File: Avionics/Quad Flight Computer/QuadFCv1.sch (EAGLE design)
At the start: 120 parts, among them J1 10104111_MICROUSBAB, J2 1050270001, Q1 DMP2035U, Q2 DMP2035U, Q3 DMP2035U, SW1 2-1437565-9, U1 TM4C123GH6PZ, U10 LTC4412, U11 AP7215-33YG-13, U2 74LVC4245APW, U3 ATMEGA32U2-MU, U4 SPI_PPM, U5 MPU-6000, U6 HMC5883LSMD, U7 MS5611-01BA, U8 74AUP1G19GW, U9 S25FL127S, X1 HWB, Y1 32.768KHZ, Y2 AWSCR-20.00CW-T, Y3 PRQC16.00SR5010X000

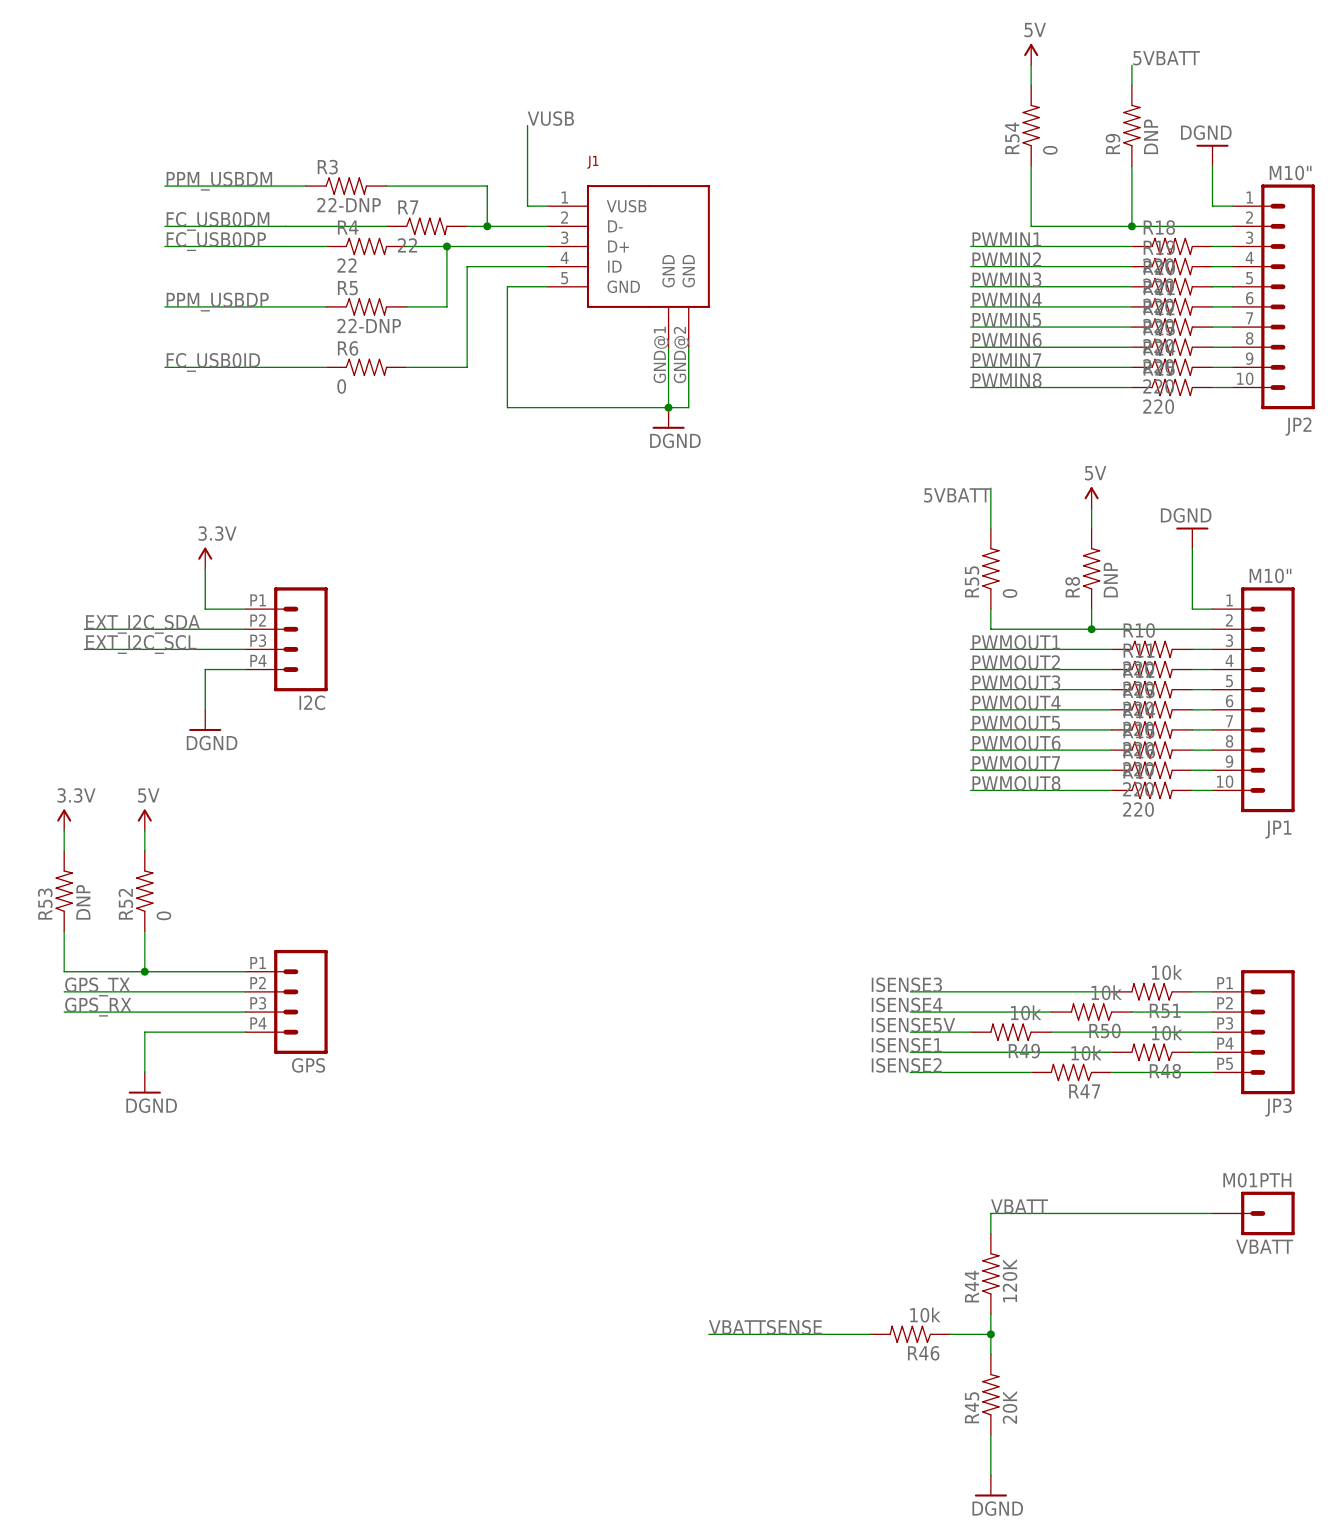
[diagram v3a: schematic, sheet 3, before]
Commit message: Changed form factor of FC to be 1.95"x1.95" to be compliant with the power distribution board. Makes stacking and interconnectivity simpler.
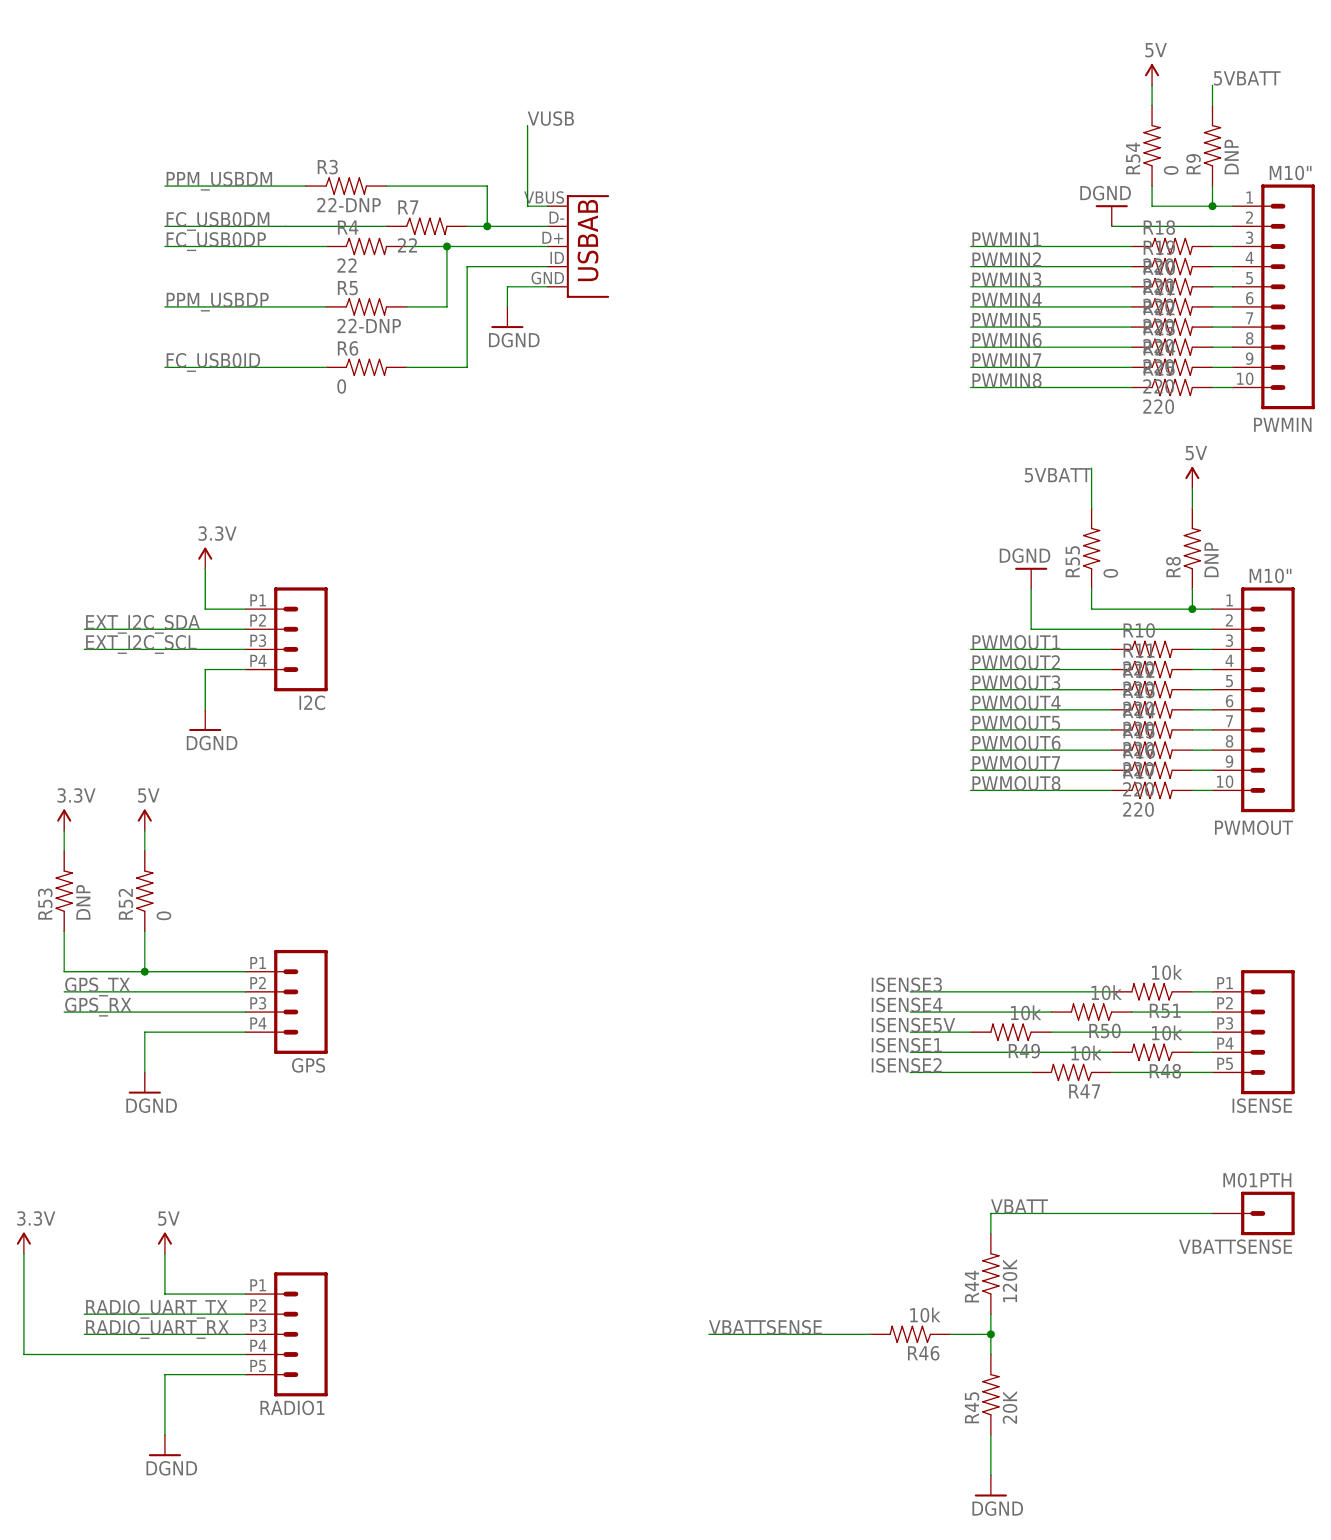
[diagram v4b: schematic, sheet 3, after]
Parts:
- removed J1: 10104111_MICROUSBAB, Shared Libraries:10104111_MICROUSBAB
- removed U4: SPI_PPM, SparkFunv2:AVR_SPI_PRG_6NS
- added RADIO1: (no value), Shared Libraries:M05DF13
- added SPI_PPM: SPI_PPM, Shared Libraries:M03X2SMD_0.05
- added U12: (no value), SparkFun-Connectors:USB-AB
- C24: device SparkFun-Capacitors:CAP0603-CAP -> SparkFun-Capacitors:CAP0402-CAP
- FC_JTAG: value M04X2 -> M04X2SMT-0.05; device SparkFun-Connectors:M04X2 -> Shared Libraries:M04X2SMT-0.05
- renumbered JP1 to PWMOUT, JP2 to PWMIN, JP3 to ISENSE, VBATT to VBATTSENSE
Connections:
- new net RADIO_UART_RX: RADIO1.3
- new net RADIO_UART_TX: RADIO1.2
- net 3.3V: now also RADIO1.4
- net 5V: now also RADIO1.1, SPI_PPM.2; no longer U4.2
- net GND: now also PWMIN.2, PWMOUT.2, RADIO1.5, SPI_PPM.6, U12.GND; no longer J1.GND, J1.GND@1, J1.GND@2, PWMIN.1, PWMOUT.1, U4.6
- net N$23: now also PWMIN.1; no longer PWMIN.2
- net N$26: now also PWMOUT.1; no longer PWMOUT.2
- net N$27: now also U12.USBID; no longer J1.ID
- net N$28: now also U12.D-; no longer J1.D-
- net N$29: now also U12.D+; no longer J1.D+
- net PPM_RST: now also SPI_PPM.5; no longer U4.5
- net PWMIN2: now also SPI_PPM.3; no longer U4.3
- net PWMIN3: now also SPI_PPM.4; no longer U4.4
- net PWMIN4: now also SPI_PPM.1; no longer U4.1
- net VUSB: now also U12.VBUS; no longer J1.VUSB
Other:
- moved on the sheet: R54, R55, R8, R9

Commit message: Consolidated entire design into single FC library. Makes everything neater and avoids package conflicts. Using any new package should be added to this library OR copied to it from another lib.
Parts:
- removed TP2: TPSQTP10SQ, testpad:TPSQTP10SQ
- added BZR: CMT-1203-SMT, QuadFCv1:CMT-1203-SMT
- added PPM: TESTPAD_TPSQTP10SQ, QuadFCv1:TESTPAD_TPSQTP10SQ
- C1, C10, C11, C12, C13, C14, C15, C16, C17, C18, C19, C2, C20, C21, C22, C23, C24, C25, C26, C3, C4, C5, C6, C7, C8, C9: device SparkFun-Capacitors:CAP0402-CAP -> QuadFCv1:CAP0402-CAP
- F1: device SparkFun:PTCSMD -> QuadFCv1:PTC0603
- FC_JTAG: device Shared Libraries:M04X2SMT-0.05 -> QuadFCv1:M04X2SMT-0.05
- GPS, I2C: device Shared Libraries:M04DF13 -> QuadFCv1:M04DF13
- ISENSE, RADIO1: device Shared Libraries:M05DF13 -> QuadFCv1:M05DF13
- J2: device Shared Libraries:1050270001 -> QuadFCv1:1050270001
- L1: device SparkFun-Passives:INDUCTOR0603 -> QuadFCv1:INDUCTOR0603
- LED1, LED2, LED3: device SparkFun:LED0603 -> QuadFCv1:LED0603
- PWMIN, PWMOUT: device SparkFun-Connectors:M10" -> QuadFCv1:M10"
- Q1, Q2, Q3: device Shared Libraries:DMP2035U -> QuadFCv1:DMP2035U
- R1, R10, R11, R12, R13, R14, R15, R16, R17, R18, R19, R2, R20, R21, R22, R23, R24, R25, R26, R27, R28, R29, R3, R30, R31, R32, R33, R34, R35, R36, R37, R38, R39, R4, R40, R41, R42, R43, R44, R45, R46, R47, R48, R49, R5, R50, R51, R52, R53, R6, R7: device SparkFun-Resistors:RESISTOR0402-RES -> QuadFCv1:RESISTOR0402-RES
- R54, R55: device SparkFun-Resistors:RESISTOR0402-RES -> QuadFCv1:RESISTOR0603-RES
- R56: device Shared Libraries:RESISTOR0402-RES -> QuadFCv1:RESISTOR0402-RES
- R8, R9: device SparkFun-Resistors:RESISTOR0805-RES -> QuadFCv1:RESISTOR0603-RES
- SPI_PPM: device Shared Libraries:M03X2SMD_0.05 -> QuadFCv1:M03X2SMD_0.05
- STANDOFF1, STANDOFF2, STANDOFF3, STANDOFF4: device SparkFun-Electromechanical:STAND-OFF -> QuadFCv1:STAND-OFF
- SW1: value 2-1437565-9 -> PTS635VL31-VERT; device Shared Libraries:2-1437565-9 -> QuadFCv1:PTS635VL31-VERT
- U1: device Shared Libraries:TM4C123GH6PZ -> QuadFCv1:TM4C123GH6PZ
- U10: device Shared Libraries:LTC4412 -> QuadFCv1:LTC4412
- U11: device Shared Libraries:AP7215-33YG-13 -> QuadFCv1:AP7215-33YG-13
- U12: device SparkFun-Connectors:USB-AB -> QuadFCv1:USB-AB
- U2: device Shared Libraries:74LVC4245APW -> QuadFCv1:74LVC4245APW
- U3: device atmel:ATMEGA8U2-MU -> QuadFCv1:ATMEGA8U2-MU
- U5: value MPU-6000 -> INVESENSE_MPU-6000; device Invesense:MPU-6000 -> QuadFCv1:INVESENSE_MPU-6000
- U6: device Shared Libraries:HMC5883LSMD -> QuadFCv1:HMC5883LSMD
- U7: device 3DRobotics:MS5611-01BA -> QuadFCv1:MS5611-01BA
- U8: device Shared Libraries:74AUP1G19GW -> QuadFCv1:74AUP1G19GW
- U9: device Shared Libraries:S25FL127S -> QuadFCv1:S25FL127S
- VBATTSENSE: device SparkFun-Connectors:M01PTH -> QuadFCv1:M01PTH
- X1: device con-molex:87758-0216 -> QuadFCv1:87758-0216
- Y1: device Shared Libraries:ECS-.327-12.5-34B -> QuadFCv1:ECS-.327-12.5-34B
- Y2: device Shared Libraries:AWSCR-20.00CW-T -> QuadFCv1:AWSCR-20.00CW-T
- Y3: device Shared Libraries:PRQC16.00SR5010X000 -> QuadFCv1:PRQC16.00SR5010X000
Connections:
- removed net VBUS: F1.2
- net FC_RESET_L: no longer SW1.1
- net GND: now also SW1.1; no longer SW1.3, SW1.4
- net PPM_OUT: now also PPM.TP; no longer TP2.TP
- net VUSB: now also F1.2

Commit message: Finished first attempt to layout EVERYTHING.
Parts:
- F1: device QuadFCv1:PTC0603 -> QuadFCv1:PTCSMD
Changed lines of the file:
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@@
 <part name="SUPPLY13" library="QuadFCv1" deviceset="5V" device=""/>
 <part name="SUPPLY14" library="QuadFCv1" deviceset="5V" device=""/>
-<part name="F1" library="QuadFCv1" deviceset="PTC" device="0603" value="500mA"/>
+<part name="F1" library="QuadFCv1" deviceset="PTC" device="SMD" value="500mA"/>
 <part name="Y3" library="QuadFCv1" deviceset="PRQC16.00SR5010X000" device=""/>
 <part name="R36" library="QuadFCv1" deviceset="RESISTOR" device="0402-RES" value="1k"/>
